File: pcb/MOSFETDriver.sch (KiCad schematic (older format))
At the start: 3 parts

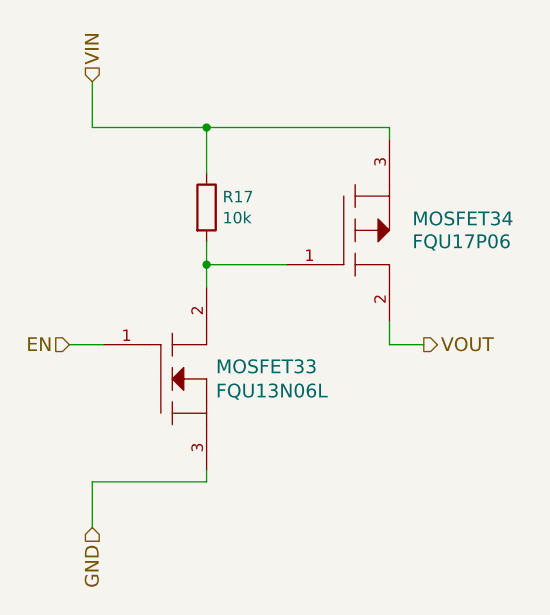
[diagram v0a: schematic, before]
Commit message: Some footprint assignments
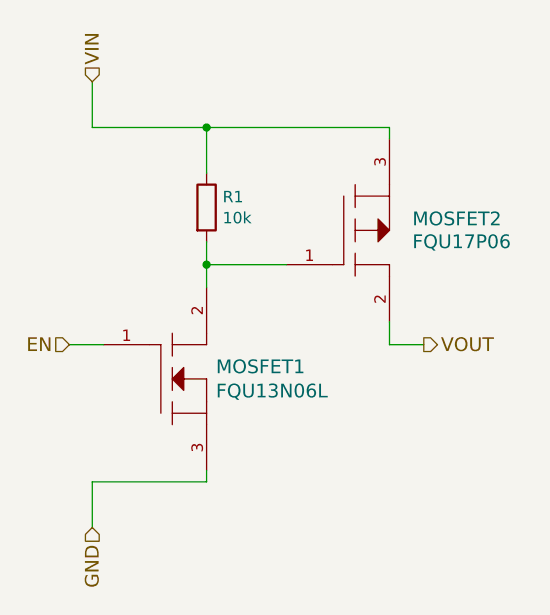
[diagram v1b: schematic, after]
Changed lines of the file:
@@
 $Descr A4 11693 8268
 encoding utf-8
-Sheet 19 19
+Sheet 2 19
 Title "Failinator"
 Date ""
@@
 AR Path="/5694859C/56946533/56877F77" Ref="MOSFET31"  Part="1"
 AR Path="/5694859C/5694653F/56877F77" Ref="MOSFET33"  Part="1"
-F 0 "MOSFET33" H 4991 4103 60  0000 L CNN
+F 0 "MOSFET1" H 4991 4103 60  0000 L CNN
 F 1 "FQU13N06L" H 4991 3997 60  0000 L CNN
 F 2 "failinator:TO-251AA" H 4650 4050 60  0001 C CNN
@@
 AR Path="/5694859C/56946533/56877F80" Ref="R16"  Part="1"
 AR Path="/5694859C/5694653F/56877F80" Ref="R17"  Part="1"
-F 0 "R17" H 5020 3346 50  0000 L CNN
+F 0 "R1" H 5020 3346 50  0000 L CNN
 F 1 "10k" H 5020 3254 50  0000 L CNN
 F 2 "Discret:R3" V 4880 3300 30  0001 C CNN
@@
 AR Path="/5694859C/56946533/56877F87" Ref="MOSFET32"  Part="1"
 AR Path="/5694859C/5694653F/56877F87" Ref="MOSFET34"  Part="1"
-F 0 "MOSFET34" H 5850 3450 60  0000 L CNN
+F 0 "MOSFET2" H 5850 3450 60  0000 L CNN
 F 1 "FQU17P06" H 5850 3350 60  0000 L CNN
 F 2 "failinator:TO-251AA" H 5450 3400 60  0001 C CNN
